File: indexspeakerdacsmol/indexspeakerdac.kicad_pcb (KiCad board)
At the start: 2 copper layers, 9 x 23.6 mm, 34 parts, among them IC1 MAX98360AEFB+T, IC2 MAX98360AEFB+T, IC3 W25Q16JVUXIQ_TR, J1 Conn_01x04_Pin, J2 Conn_01x04_Pin, U1 RP2040, U2 MIC5317-3.3xM5, Y1 Crystal_GND24

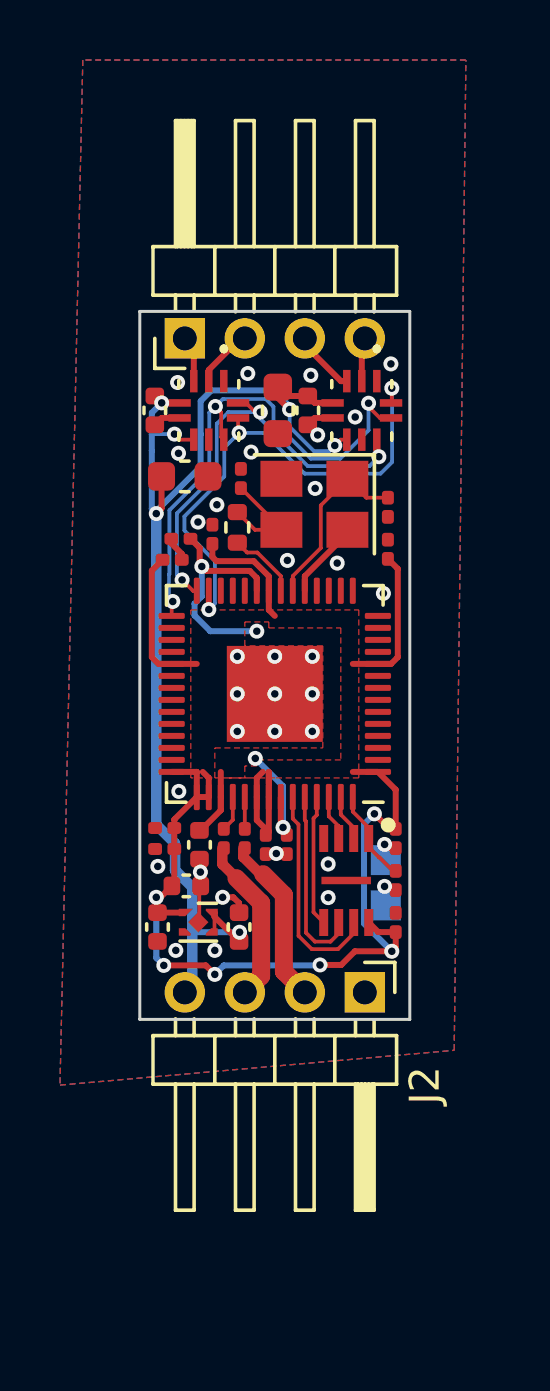
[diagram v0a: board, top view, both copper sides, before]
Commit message: add usb c + bom
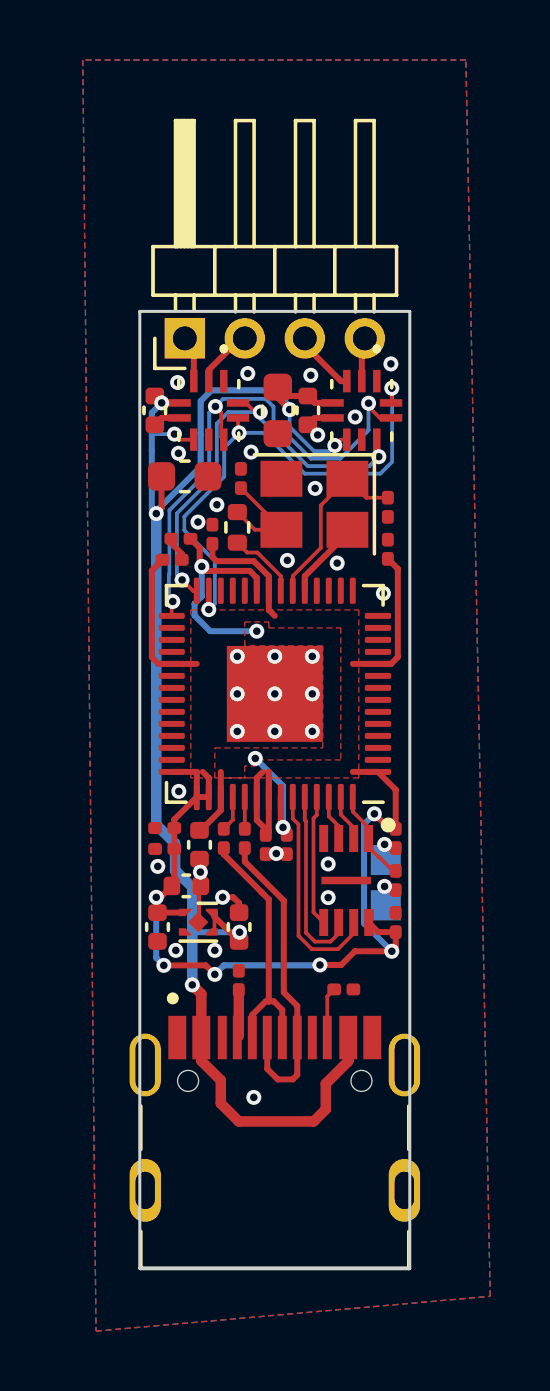
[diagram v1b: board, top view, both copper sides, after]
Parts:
- removed J2: Conn_01x04_Pin, Connector_PinHeader_2.00mm:PinHeader_1x04_P2.00mm_Horizontal
- added J3: TYPE-C-31-M-12, footprint:HRO_TYPE-C-31-M-12, F.Cu at (140.0, 111.1)
- added R5: 5K1, Resistor_SMD:R_0201_0603Metric, F.Cu at (138.8, 104.1)
- added R6: 5K1, Resistor_SMD:R_0201_0603Metric, F.Cu at (142.3, 104.4)
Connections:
- R2 pad 1: Net-(J2-Pin_3) -> /USB_DN
- R3 pad 1: Net-(J2-Pin_2) -> /USB_DP
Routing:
- net VCC: track 41.8 -> 52.4 mm, vias 6 -> 7
- net /USB_DP: track 0.00 -> 10.5 mm
- net /USB_DN: track 0.00 -> 8.78 mm
- net Net-(J2-Pin_2): track 5.71 -> 0.00 mm
- net Net-(J2-Pin_3): track 5.57 -> 0.00 mm
- net Net-(J3-CC2): track 0.00 -> 1.70 mm
- net Net-(J3-CC1): track 0.00 -> 1.61 mm
- net GND: vias 33 -> 34
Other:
- board size 9 x 23.6 mm -> 9 x 31.9 mm
